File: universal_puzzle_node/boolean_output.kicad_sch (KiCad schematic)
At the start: 6 parts

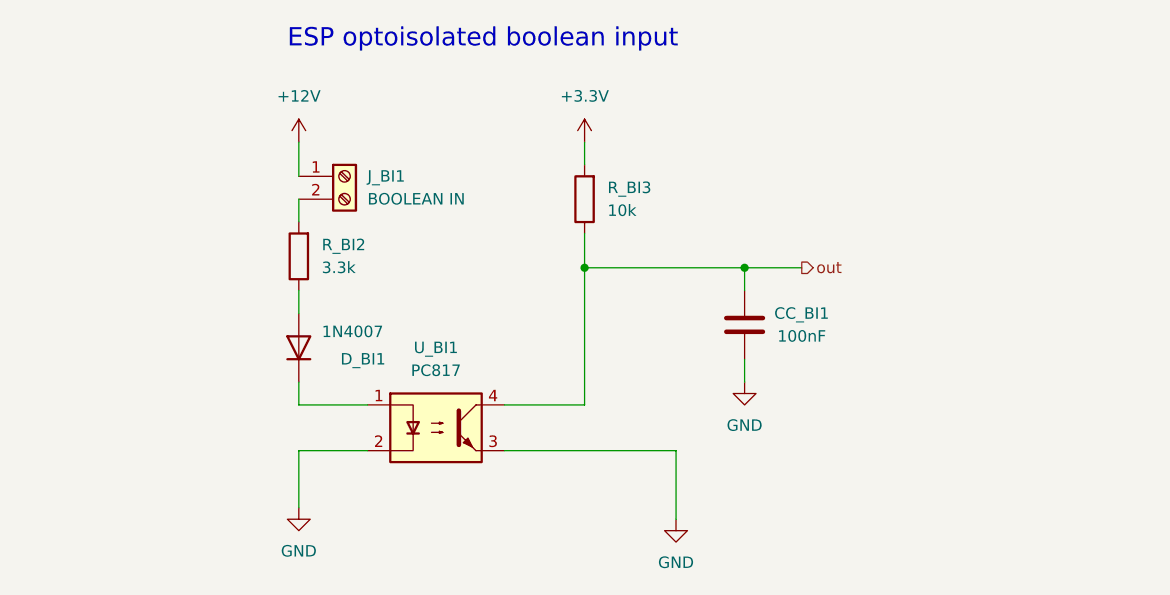
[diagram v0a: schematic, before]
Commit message: chore: rename to universal puzzle node everywhere
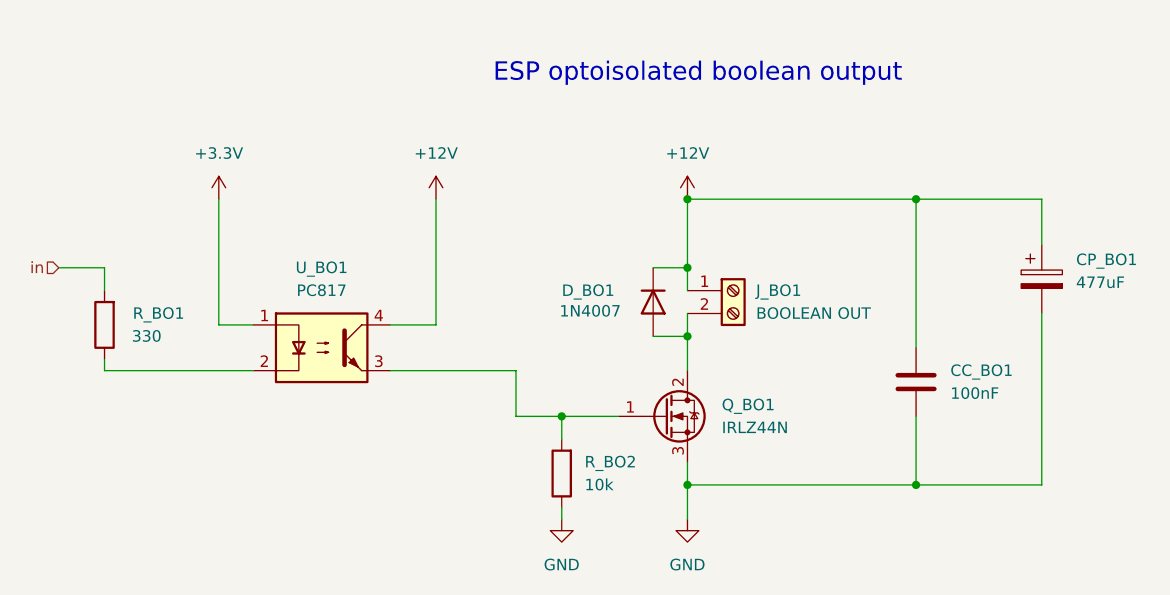
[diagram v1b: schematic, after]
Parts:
- removed CC_BI1: 100nF, Capacitor_THT:C_Disc_D5.0mm_W2.5mm_P5.00mm, symbol Device:C
- removed D_BI1: 1N4007, Diode_THT:D_DO-41_SOD81_P10.16mm_Horizontal, symbol Diode:1N4007
- removed J_BI1: BOOLEAN IN, TerminalBlock_Phoenix:TerminalBlock_Phoenix_MKDS-1,5-2-5.08_1x02_P5.08mm_Horizontal, symbol Connector:Screw_Terminal_01x02
- removed R_BI2: 3.3k, Resistor_THT:R_Axial_DIN0207_L6.3mm_D2.5mm_P10.16mm_Horizontal, symbol Device:R
- removed R_BI3: 10k, Resistor_THT:R_Axial_DIN0207_L6.3mm_D2.5mm_P10.16mm_Horizontal, symbol Device:R
- removed U_BI1: PC817, Package_DIP:DIP-4_W7.62mm, symbol Isolator:PC817
- added CC_BO1: 100nF, Capacitor_THT:C_Disc_D5.0mm_W2.5mm_P5.00mm, symbol Device:C
- added CP_BO1: 477uF, Capacitor_THT:CP_Radial_D10.0mm_P5.00mm, symbol Device:C_Polarized
- added D_BO1: 1N4007, Diode_THT:D_DO-41_SOD81_P10.16mm_Horizontal, symbol Diode:1N4007
- added J_BO1: BOOLEAN OUT, TerminalBlock_Phoenix:TerminalBlock_Phoenix_MKDS-1,5-2-5.08_1x02_P5.08mm_Horizontal, symbol Connector:Screw_Terminal_01x02
- added Q_BO1: IRLZ44N, Package_TO_SOT_THT:TO-220-3_Vertical, symbol Transistor_FET:IRLZ44N
- added R_BO1: 330, Resistor_THT:R_Axial_DIN0207_L6.3mm_D2.5mm_P10.16mm_Horizontal, symbol Device:R
- added R_BO2: 10k, Resistor_THT:R_Axial_DIN0207_L6.3mm_D2.5mm_P10.16mm_Horizontal, symbol Device:R
- added U_BO1: PC817, Package_DIP:DIP-4_W7.62mm, symbol Isolator:PC817
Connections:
- net +12V: now also CC_BO1.2, CP_BO1.1, D_BO1.1 (K), J_BO1.1 (Pin_1), U_BO1.4
- net +3.3V: now also U_BO1.1
- net GND: now also CC_BO1.1, CP_BO1.2, Q_BO1.3 (S), R_BO2.1
- new net: D_BO1.2 (A), J_BO1.2 (Pin_2), Q_BO1.2 (D)
- new net: R_BO1.1, U_BO1.2
- new net: Q_BO1.1 (G), R_BO2.2, U_BO1.3
- new net in: R_BO1.2
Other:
- note added: "ESP optoisolated boolean output"
- note removed: "ESP optoisolated boolean input"
